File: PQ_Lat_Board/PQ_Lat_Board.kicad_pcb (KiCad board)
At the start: 6 copper layers, 64 x 52 mm, 31 parts, among them IC1 TCN75AVOA713, J1 53261-1471, J2 Conn_01x08_MountingPin, J3 53261-0271

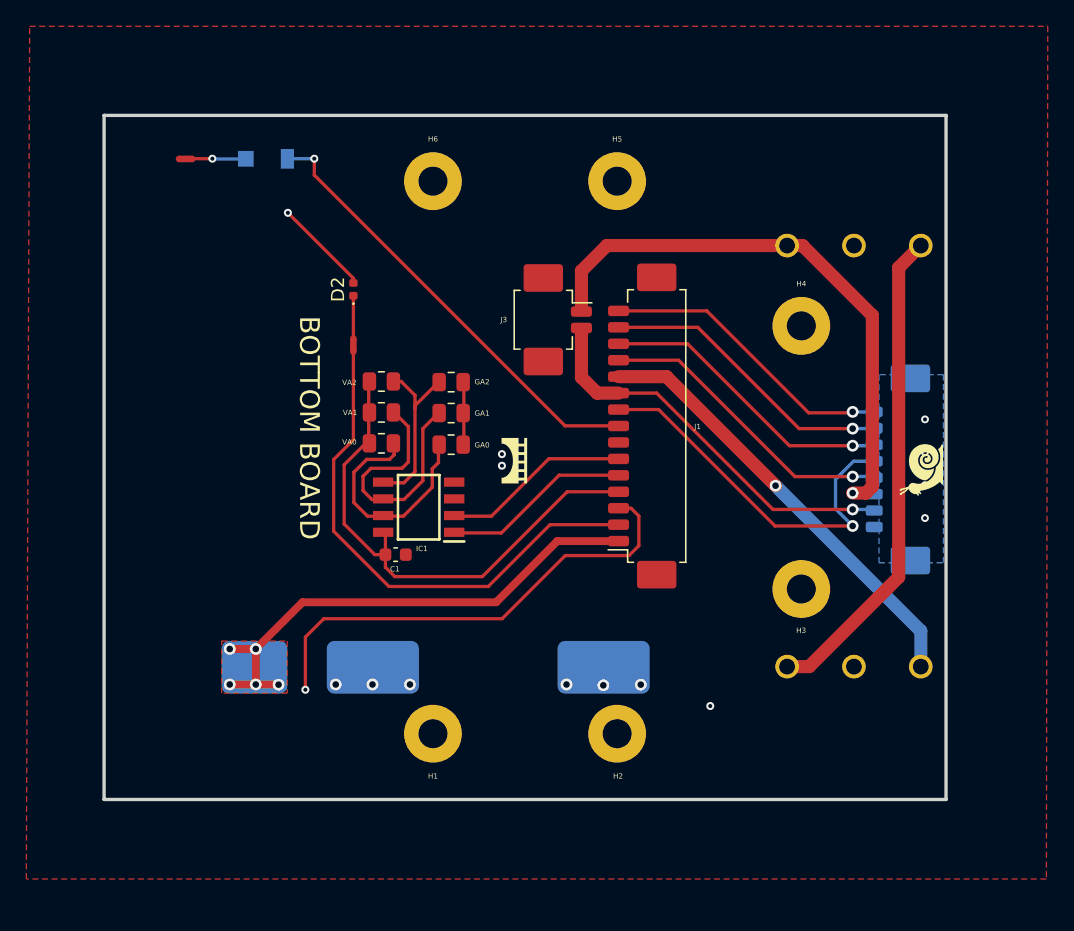
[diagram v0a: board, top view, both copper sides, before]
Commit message: fix mirroring of Lightricity's solar cells
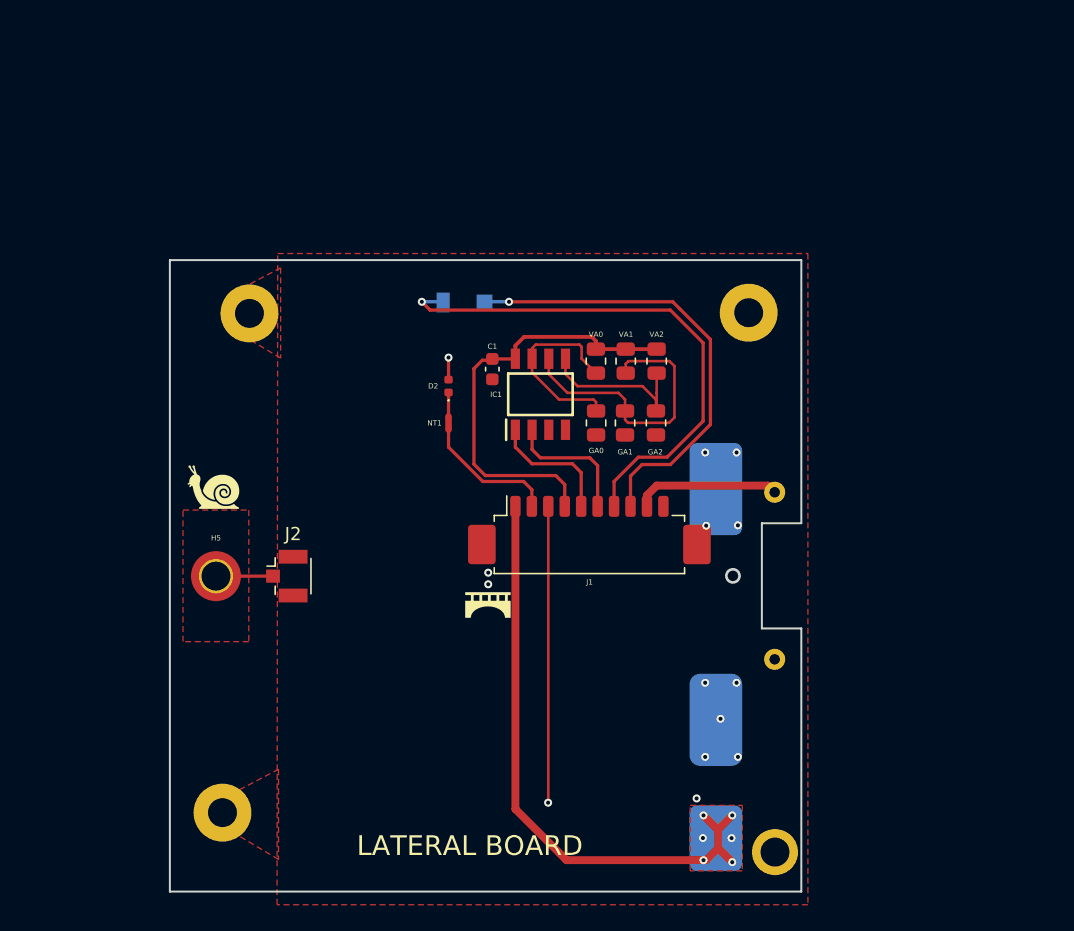
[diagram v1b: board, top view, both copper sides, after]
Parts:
- removed H6: MountingHole_Pad, MountingHole:MountingHole_2.2mm_M2_Pad
- removed J3: 53261-0271, Connector_Molex:Molex_PicoBlade_53261-0271_1x02-1MP_P1.25mm_Horizontal
- removed KS1: D2F-01L-A1, -nsl_miscellaneous:D2FLA1
- removed KS2: D2F-01L-A, -nsl_miscellaneous:D2FLA
- removed NT2: NetTie_2, NetTie:NetTie-2_SMD_Pad0.5mm
- added Annotation8: GRSS, symbols-nsl:GRSS, B.Cu at (118.3, 52.1)
- added THT1: 7.5, Resistor_THT:R_Axial_DIN0309_L9.0mm_D3.2mm_P12.70mm_Horizontal, B.Cu at (121.0, 59.6)
- Annotation1: footprint -nsl_symbols:GRSS -> -nsl_symbols:Bridgemaker; moved to F.Cu
- Annotation2: footprint -nsl_symbols:IEEE_logo -> symbols-nsl:snail; moved to F.Cu
- Annotation3: value Silkscreen_Annotation -> LOGO; footprint -nsl_symbols:UPC_positiu -> symbols-nsl:pocat-lektron
- Annotation4: value Silkscreen_Annotation -> Logo lektron; footprint -nsl_symbols:Telecos -> symbols-nsl:logo_pq
- Annotation5: value Silkscreen_Annotation -> telecos; footprint -nsl_symbols:Bridgemaker -> symbols-nsl:Telecos; moved to B.Cu
- Annotation6: value snail -> telecos; footprint symbols-nsl:snail -> symbols-nsl:NSL-small; moved to B.Cu
- Annotation7: value pocat lektron -> IEEE; footprint symbols-nsl:pocat-lektron -> symbols-nsl:UPC_small
- H5: footprint MountingHole:MountingHole_2.2mm_M2_Pad -> MountingHole:MountingHole_2.2mm_M2_DIN965_Pad_TopOnly
- J1: value 53261-1471 -> Conn_01x11_MountingPin; footprint Connector_Molex:Molex_PicoBlade_53261-1571_1x15-1MP_P1.25mm_Horizontal -> Connector_Molex:Molex_PicoBlade_53261-1071_1x10-1MP_P1.25mm_Horizontal
- J2: value Conn_01x08_MountingPin -> Conn_Coaxial; footprint Connector_Molex:Molex_PicoBlade_53398-0871_1x08-1MP_P1.25mm_Vertical -> Connector_Coaxial:U.FL_Hirose_U.FL-R-SMT-1_Vertical; moved to F.Cu
- SC1: footprint power-nsl:Lighttricity_S3040_CIC_ -> power-nsl:Lighttricity_S3040_CIC
- moved Annotation6 57.8 mm to (76.9, 75.0)
- moved H4 57.5 mm to (79.0, 84.0)
- moved Annotation7 47.7 mm to (80.3, 72.9), turned to 90 degrees
- moved J2 46.6 mm to (83.9, 66.0), turned to 0 degrees
- moved Annotation4 43.2 mm to (78.8, 57.0), turned to 180 degrees
- moved H5 42.8 mm to (78.5, 66.0)
- moved SC1 39.9 mm to (113.5, 88.9), turned to 90 degrees
- moved H1 34.9 mm to (81.0, 46.0)
- moved Annotation3 34.7 mm to (108.9, 45.1), turned to 180 degrees
- moved H2 33.5 mm to (119.0, 46.0)
- moved Annotation1 24.7 mm to (99.1, 68.3), turned to 0 degrees
- moved VA2 21.0 mm to (112.0, 49.7), turned to 90 degrees
- moved Annotation2 20.1 mm to (78.3, 59.3), turned to 0 degrees
- moved H3 20.1 mm to (121.0, 87.0)
- moved D1 19.1 mm to (97.7, 45.3), turned to 180 degrees
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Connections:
- net /MAG-Y renamed /ADCS
- net /SOLAR_Y renamed /SOLAR
- D1 pad 1: /PH+ -> /PH-
- D1 pad 2: /PH- -> /PH+
- H5 pad 1: GND -> /Antenna Connector
- J1 pad 10: /BATT- -> GND
- J1 pad 7: GND -> /PH-
- J1 pad 9: /SWO -> /BURNCOMMS
- J2 pad 1: /VCC_Umbilical -> /Antenna Connector
- J2 pad 2: /SWDIO -> GND
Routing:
- net /BATT+: track 44.2 -> 0.00 mm, vias 1 -> 0
- net Net-(KS1-NC): track 37.2 -> 0.00 mm
- net /PH-: track 4.09 -> 40.8 mm
- net /KILLSWITCH+: track 33.7 -> 0.00 mm, vias 1 -> 0
- net /BATT-: track 29.7 -> 0.00 mm, vias 1 -> 0
- net /ADCS: track 39.6 -> 10.3 mm
- net /SWO: track 29.1 -> 0.00 mm, vias 1 -> 0
- net /NRST: track 23.1 -> 0.00 mm, vias 1 -> 0
- net /VCC_Umbilical: track 22.7 -> 0.00 mm, vias 1 -> 0
- net /SWCLK: track 22.7 -> 0.00 mm, vias 1 -> 0
- net /SWDIO: track 22.6 -> 0.00 mm, vias 1 -> 0
- net /BURNCOMMS: track 0.00 -> 11.1 mm
- net /VCC_MAG: track 9686.7 -> 9694.4 mm
- net /SOLAR: track 39.4 -> 46.4 mm, vias 5 -> 6
- net /VCC: track 39.1 -> 32.6 mm
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- added copper zone on F.Cu, net /Antenna Connector
- removed copper zone on B.Cu, net GND
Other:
- board size 64 x 52 mm -> 48 x 48 mm
- board text added: "+Y"
- board text added: "-Y"
- board text added: "LATERAL BOARD"
- board text removed: "+X"
- board text removed: "+Z"
- board text removed: "-X"
- board text removed: "BOTTOM BOARD"
